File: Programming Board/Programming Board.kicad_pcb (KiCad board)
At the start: 2 copper layers, 41.3 x 36.2 mm, 7 parts, among them J1 TEST_1P, J2 SPOX-5, SW1 SW_Push, SW2 SW_DIP_x01, U1 DB20M, U2 Board_Edge_5x2x2.54

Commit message: PCB update
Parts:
- added REF**: via, WARG-kicad:via, F.Cu at (184.8, 140.3)
- added REF**: via, WARG-kicad:via, F.Cu at (188.0, 137.2)
- SW1: footprint WARG KiCAD:Programmer_ResetButton -> Programmer_ResetButton
- SW2: footprint WARG KiCAD:Programming_Board_Switch -> Programming_Board_Switch
- U1: footprint WARG-kicad:Board_Edge_female -> WARG KiCAD:Board_Edge_10x2x2.54
- moved SW2 4.02 mm to (179.0, 118.3)
- moved SW1 1.80 mm to (192.0, 130.3)
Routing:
- net GND: track 48.4 -> 79.2 mm
- net MCUVDD: track 64.7 -> 85.0 mm
- net /3V3: track 117.6 -> 125.7 mm
- net SWDIO: track 57.7 -> 58.9 mm
- added copper zone on F.Cu, net MCUVDD
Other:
- board size 41.3 x 36.2 mm -> 41.3 x 40.6 mm

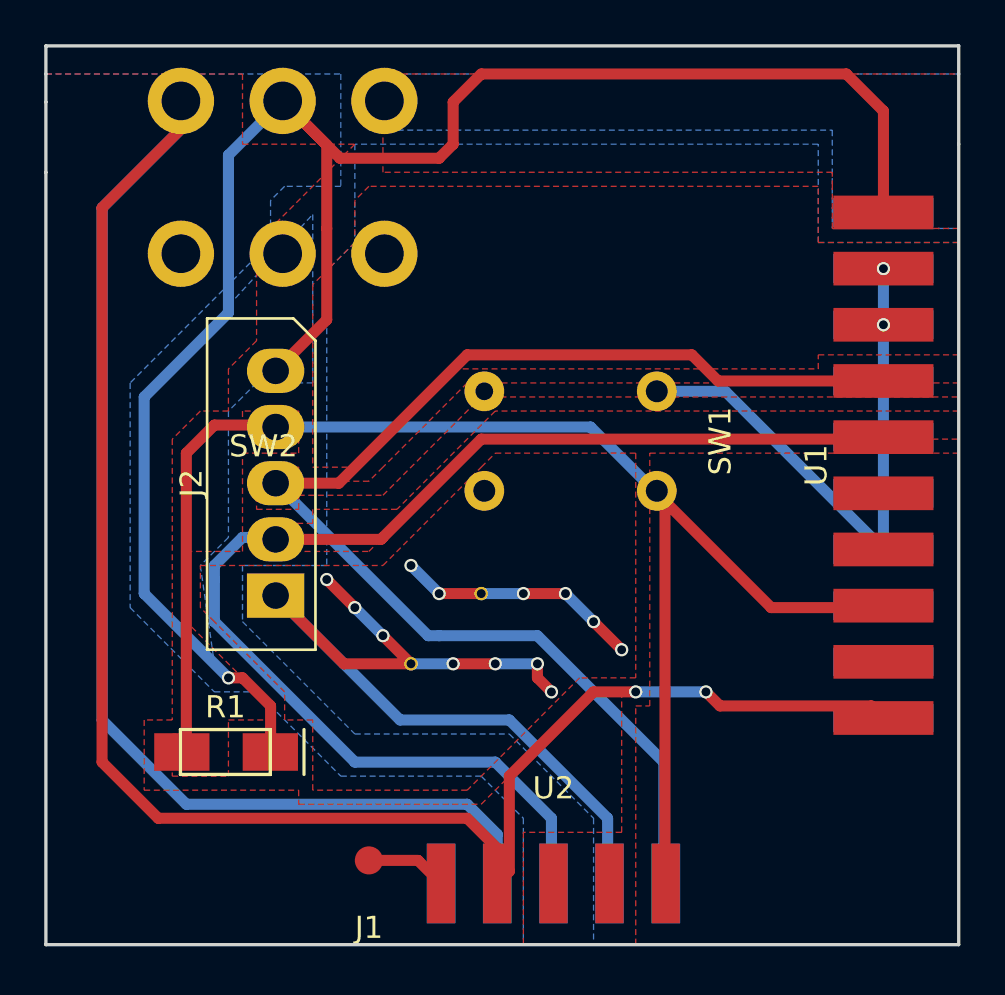
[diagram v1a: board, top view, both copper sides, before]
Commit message: Fix pad connections
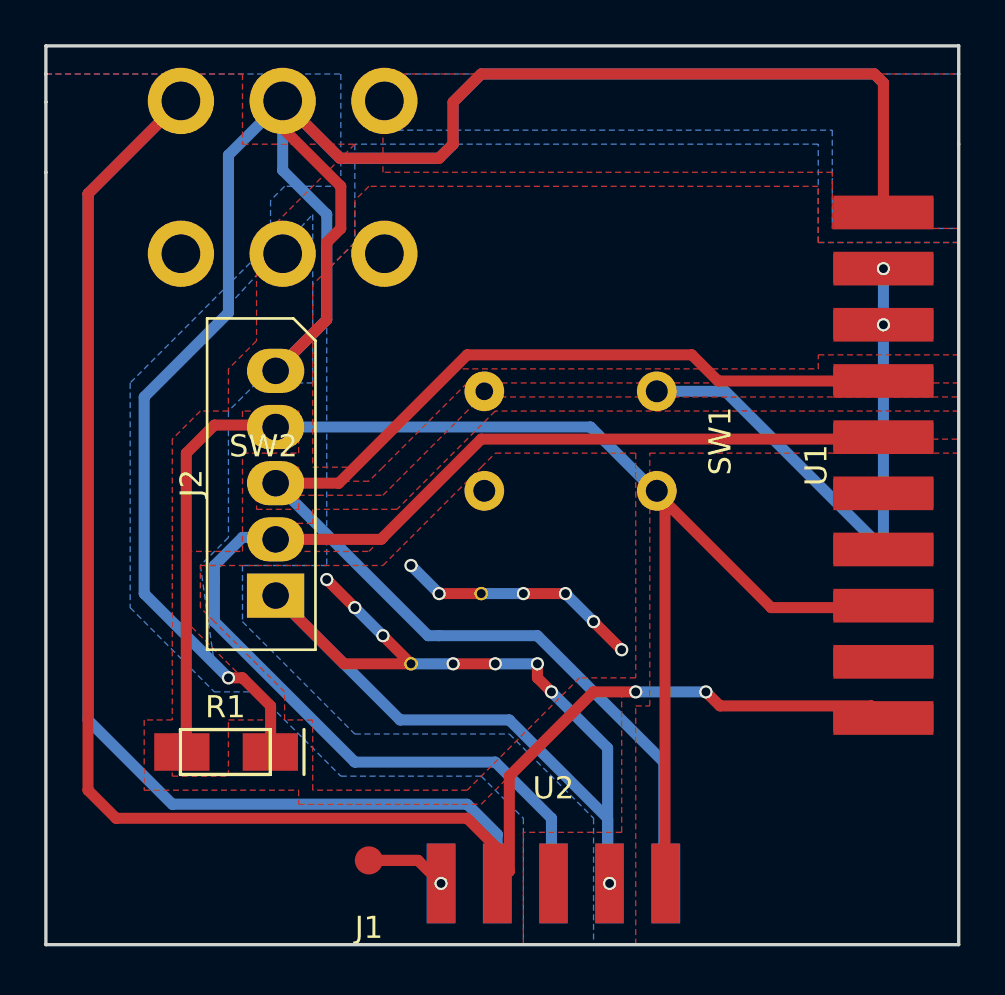
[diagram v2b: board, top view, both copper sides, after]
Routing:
- net MCUVDD: track 85.0 -> 137.2 mm
- net GND: track 79.2 -> 88.8 mm, vias 17 -> 18
- net /3V3: track 125.7 -> 130.7 mm
- net Net-(J1-Pad1): track 3.70 -> 5.92 mm, vias 0 -> 1
